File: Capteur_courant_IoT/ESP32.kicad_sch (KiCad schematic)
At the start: 7 parts, among them U2 ESP32-WROOM-32E, U4 ADS1015IDGS

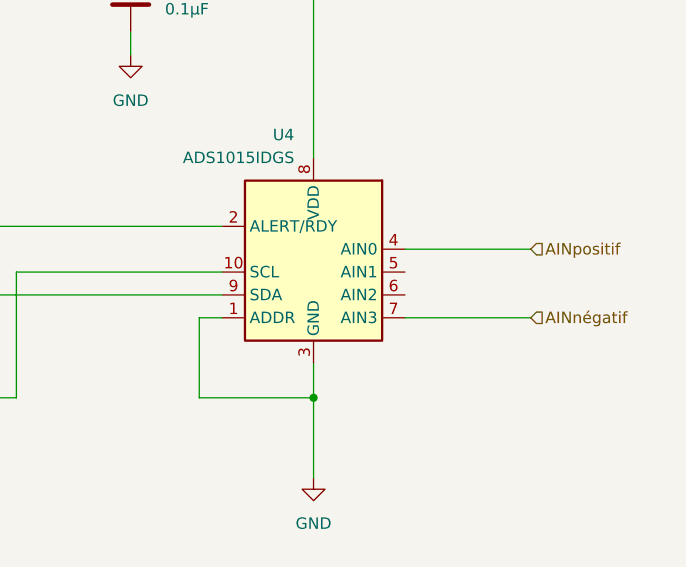
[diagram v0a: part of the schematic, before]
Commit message: ajout bornier pour capteur de courant
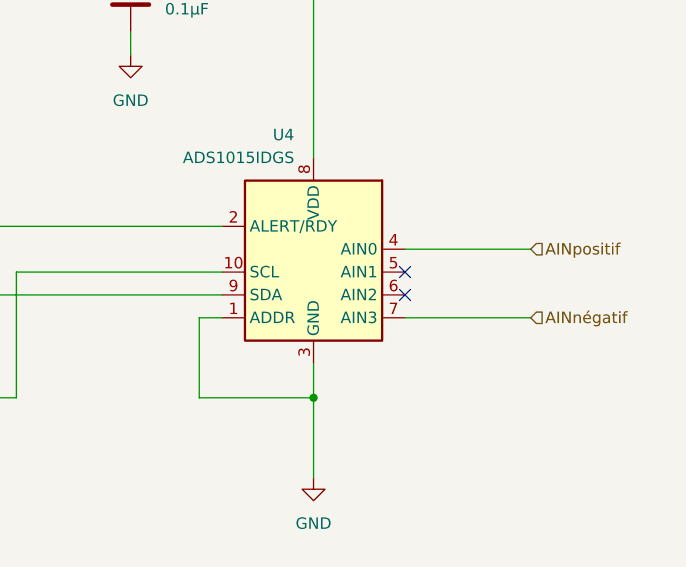
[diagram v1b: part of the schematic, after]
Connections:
- no-connect marks 15 -> 17
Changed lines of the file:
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@@
+	)
+	(no_connect
+		(at 214.63 95.25)
 	)
 	(no_connect
@@
 	)
 	(no_connect
+		(at 214.63 92.71)
+	)
+	(no_connect

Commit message: correction des points évoqués
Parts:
- added C11: C, Capacitor_SMD:C_0603_1608Metric, symbol Device:C
- added R15: 0R, Resistor_SMD:R_0805_2012Metric, symbol Device:R
- added R20: R, Resistor_SMD:R_0805_2012Metric, symbol Device:R
- C1, C10, C2: footprint (none) -> Capacitor_SMD:C_0603_1608Metric
- R10, R13: footprint (none) -> Resistor_SMD:R_0805_2012Metric
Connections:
- net AINnégatif: now also R15.1
- net AINpositif: now also R20.2; no longer U4.4 (AIN0)
- net GND: now also C11.2, R15.2
- new net: C11.1, R20.1, U4.4 (AIN0)

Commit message: V100
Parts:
- added R3: 0R, Resistor_SMD:R_0805_2012Metric, symbol Device:R
- C1, C10, C11, C2: footprint Capacitor_SMD:C_0603_1608Metric -> Capacitor_SMD:C_0805_2012Metric
- U2: footprint RF_Module:ESP32-WROOM-32D -> RF_Module:ESP32-WROOM-32E
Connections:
- net AINnégatif: now also R3.2; no longer U4.7 (AIN3)
- net RXD0 renamed RXD0_cp2102 -- TXD0_ESP32
- net TXD0 renamed TXD0_cp2102 -- RXD0_ESP32
- new net: R3.1, U4.7 (AIN3)
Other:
- note added: "A dimensionner en fonction du cas d'application"
- moved on the sheet: C10, C11, R15, R20, U4
